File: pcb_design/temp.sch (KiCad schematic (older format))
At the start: 3 parts

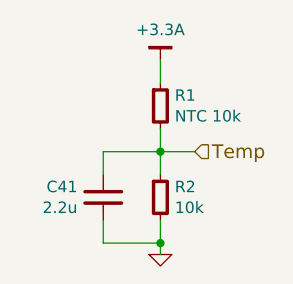
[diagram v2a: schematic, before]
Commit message: Completed some part numbers
Signed-off-by: Marcos Chaparro <mchaparro@paltatech.com>
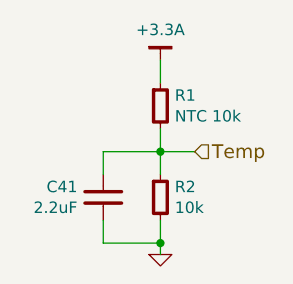
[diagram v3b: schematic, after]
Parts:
- C41: value 2.2u -> 2.2uF; MFR (none) -> Murata Electronics North America; MPN (none) -> GRM188R71A225KE15D; SPN (none) -> 490-4520-1-ND; SPR (none) -> Digikey
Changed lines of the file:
@@
 U 1 1 5426DB25
 P 4400 4200
-F 0 "#PWR38" H 4400 4200 30  0001 C CNN
-F 1 "GND" H 4400 4130 30  0001 C CNN
-F 2 "" H 4400 4200 60  0000 C CNN
-F 3 "" H 4400 4200 60  0000 C CNN
+F 0 "#PWR38" H 4400 4200 30 0001 C CNN
+F 1 "GND" H 4400 4130 30 0001 C CNN
+F 2 "" H 4400 4200 60 0000 C CNN
+F 3 "" H 4400 4200 60 0000 C CNN
 	1    4400 4200
 	1    0    0    -1
 $EndComp
-Wire Wire Line
-	4400 4050 4400 4200
-Wire Wire Line
-	4150 4150 4400 4150
-Connection ~ 4400 4150
-Wire Wire Line
-	4400 3650 4400 3850
-Wire Wire Line
-	4150 3750 4550 3750
-Connection ~ 4400 3750
-Wire Wire Line
-	4400 3350 4400 3450
-Text HLabel 4550 3750 2    60   Input ~ 0
-Temp
 $Comp
 L R-0603 R2
 U 1 1 588BA5AA
 P 4400 3950
-F 0 "R2" H 4463 3996 50  0000 L CNN
-F 1 "10k" H 4463 3905 50  0000 L CNN
-F 2 "IPC7351-Nominal:RESC1608X50" H 4400 3950 50  0001 C CNN
-F 3 "" H 4400 4000 60  0000 C CNN
-F 4 "RES SMD 1k 5% [0603]" H 5150 4500 60  0001 C CNN "BOM"
+F 0 "R2" H 4463 3996 50 0000 L CNN
+F 1 "10k" H 4463 3905 50 0000 L CNN
+F 2 "IPC7351-Nominal:RESC1608X50" H 4400 3950 50 0001 C CNN
+F 3 "" H 4400 4000 60 0000 C CNN
+F 4 "RES SMD 1k 5% [0603]" H 5150 4500 60 0001 C CNN "BOM"
+F 5 "" H 0 0 50 0001 C CNN "MFR"
+F 6 "" H 0 0 50 0001 C CNN "MPN"
+F 7 "" H 0 0 50 0001 C CNN "SPR"
+F 8 "" H 0 0 50 0001 C CNN "SPN"
+F 9 "" H 0 0 50 0001 C CNN "SPURL"
 	1    4400 3950
 	1    0    0    -1
@@
 U 1 1 588BA6A5
 P 4400 3550
-F 0 "R1" H 4463 3596 50  0000 L CNN
-F 1 "NTC 10k" H 4463 3505 50  0000 L CNN
-F 2 "IPC7351-Nominal:RESC1608X50" H 4400 3550 50  0001 C CNN
-F 3 "" H 4400 3600 60  0000 C CNN
-F 4 "RES SMD 1k 5% [0603]" H 5150 4100 60  0001 C CNN "BOM"
+F 0 "R1" H 4463 3596 50 0000 L CNN
+F 1 "NTC 10k" H 4463 3505 50 0000 L CNN
+F 2 "IPC7351-Nominal:RESC1608X50" H 4400 3550 50 0001 C CNN
+F 3 "" H 4400 3600 60 0000 C CNN
+F 4 "RES SMD 1k 5% [0603]" H 5150 4100 60 0001 C CNN "BOM"
+F 5 "" H 0 0 50 0001 C CNN "MFR"
+F 6 "" H 0 0 50 0001 C CNN "MPN"
+F 7 "" H 0 0 50 0001 C CNN "SPR"
+F 8 "" H 0 0 50 0001 C CNN "SPN"
+F 9 "" H 0 0 50 0001 C CNN "SPURL"
 	1    4400 3550
 	1    0    0    -1
@@
 U 1 1 588BA7A2
 P 4150 3950
-F 0 "C41" H 4263 3996 50  0000 L CNN
-F 1 "2.2u" H 4263 3905 50  0000 L CNN
-F 2 "IPC7351-Nominal:CAPC1608X55" H 4150 3950 50  0001 C CNN
-F 3 "" H 4140 3925 60  0000 C CNN
-F 4 "CAP MLCC 100pF C0G 50V 5% [0603]" H 4950 4500 60  0001 C CNN "BOM"
+F 0 "C41" H 4263 3996 50 0000 L CNN
+F 1 "2.2uF" H 4263 3905 50 0000 L CNN
+F 2 "IPC7351-Nominal:CAPC1608X55" H 4150 3950 50 0001 C CNN
+F 3 "http://www.murata.com/~/media/webrenewal/support/library/catalog/products/capacitor/mlcc/c02e.ashx" H 4140 3925 60 0001 C CNN
+F 4 "CAP MLCC 100pF C0G 50V 5% [0603]" H 4950 4500 60 0001 C CNN "BOM"
+F 5 "Murata Electronics North America" H 0 0 50 0001 C CNN "MFR"
+F 6 "GRM188R71A225KE15D" H 0 0 50 0001 C CNN "MPN"
+F 7 "Digikey" H 0 0 50 0001 C CNN "SPR"
+F 8 "490-4520-1-ND" H 0 0 50 0001 C CNN "SPN"
+F 9 "" H 0 0 50 0001 C CNN "SPURL"
 	1    4150 3950
 	-1   0    0    -1
 $EndComp
+$Comp
+L +3.3A #PWR37
+U 1 1 588BA405
+P 4400 3350
+F 0 "#PWR37" H 0 100 30 0001 C CNN
+F 1 "+3.3A" H 4400 3483 50 0000 C CNN
+F 2 "" H 0 50 60 0000 C CNN
+F 3 "" H 0 50 60 0000 C CNN
+	1    4400 3350
+	1    0    0    -1
+$EndComp
+Text HLabel 4550 3750 2    60   Input ~ 0
+Temp
+Wire Wire Line
+	4400 4050 4400 4200
+Wire Wire Line
+	4150 4150 4400 4150
+Wire Wire Line
+	4400 3650 4400 3850
+Wire Wire Line
+	4150 3750 4550 3750
+Wire Wire Line
+	4400 3350 4400 3450
 Wire Wire Line
 	4150 3850 4150 3750
 Wire Wire Line
 	4150 4050 4150 4150
-$Comp
-L +3.3A #PWR37
-U 1 1 588BA405
-P 4400 3350
-F 0 "#PWR37" H 0   100 30  0001 C CNN
-F 1 "+3.3A" H 4400 3483 50  0000 C CNN
-F 2 "" H 0   50  60  0000 C CNN
-F 3 "" H 0   50  60  0000 C CNN
-	1    4400 3350
-	1    0    0    -1
-$EndComp
+Connection ~ 4400 4150
+Connection ~ 4400 3750
 $EndSCHEMATC

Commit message: Completed part number, manufacturer, etc fields. Simulated analog conditioning
Signed-off-by: Marcos Chaparro <mchaparro@paltatech.com>
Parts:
- R1: MFR (none) -> Murata Electronics North America; MPN (none) -> NCP18XH103F03RB; SPN (none) -> 490-4800-1-ND; SPR (none) -> Digikey
- R2: MFR (none) -> Yageo; MPN (none) -> RC0603FR-0710KL; SPN (none) -> 311-10.0KHRCT-ND; SPR (none) -> Digikey
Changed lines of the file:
@@
 F 1 "10k" H 4463 3905 50 0000 L CNN
 F 2 "IPC7351-Nominal:RESC1608X50" H 4400 3950 50 0001 C CNN
-F 3 "" H 4400 4000 60 0000 C CNN
+F 3 "" H 4400 4000 60 0001 C CNN
 F 4 "RES SMD 1k 5% [0603]" H 5150 4500 60 0001 C CNN "BOM"
-F 5 "" H 0 0 50 0001 C CNN "MFR"
-F 6 "" H 0 0 50 0001 C CNN "MPN"
-F 7 "" H 0 0 50 0001 C CNN "SPR"
-F 8 "" H 0 0 50 0001 C CNN "SPN"
+F 5 "Yageo" H 0 0 50 0001 C CNN "MFR"
+F 6 "RC0603FR-0710KL" H 0 0 50 0001 C CNN "MPN"
+F 7 "Digikey" H 0 0 50 0001 C CNN "SPR"
+F 8 "311-10.0KHRCT-ND" H 0 0 50 0001 C CNN "SPN"
 F 9 "" H 0 0 50 0001 C CNN "SPURL"
 	1    4400 3950
@@
 F 1 "NTC 10k" H 4463 3505 50 0000 L CNN
 F 2 "IPC7351-Nominal:RESC1608X50" H 4400 3550 50 0001 C CNN
-F 3 "" H 4400 3600 60 0000 C CNN
+F 3 "" H 4400 3600 60 0001 C CNN
 F 4 "RES SMD 1k 5% [0603]" H 5150 4100 60 0001 C CNN "BOM"
-F 5 "" H 0 0 50 0001 C CNN "MFR"
-F 6 "" H 0 0 50 0001 C CNN "MPN"
-F 7 "" H 0 0 50 0001 C CNN "SPR"
-F 8 "" H 0 0 50 0001 C CNN "SPN"
+F 5 "Murata Electronics North America" H 0 0 50 0001 C CNN "MFR"
+F 6 "NCP18XH103F03RB" H 0 0 50 0001 C CNN "MPN"
+F 7 "Digikey" H 0 0 50 0001 C CNN "SPR"
+F 8 "490-4800-1-ND" H 0 0 50 0001 C CNN "SPN"
 F 9 "" H 0 0 50 0001 C CNN "SPURL"
 	1    4400 3550

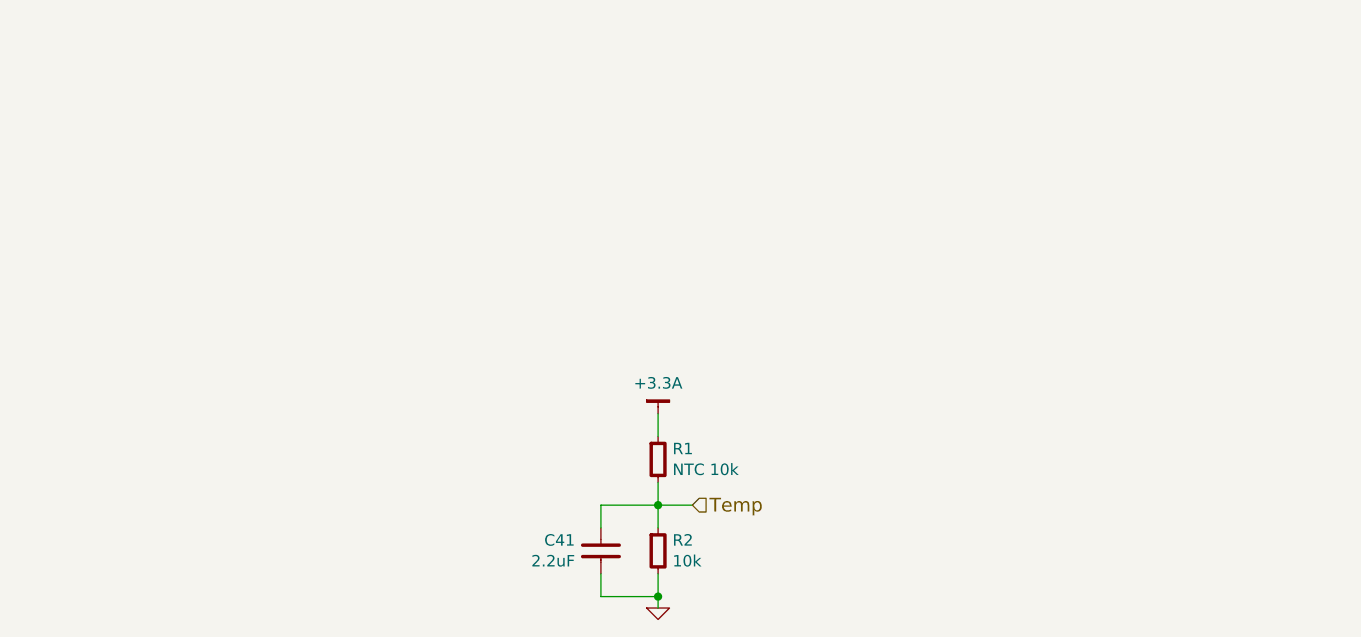
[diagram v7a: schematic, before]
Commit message: Added RC filter to FAULT line to prevent noise triggering it
Signed-off-by: Marcos Chaparro <mchaparro@paltatech.com>
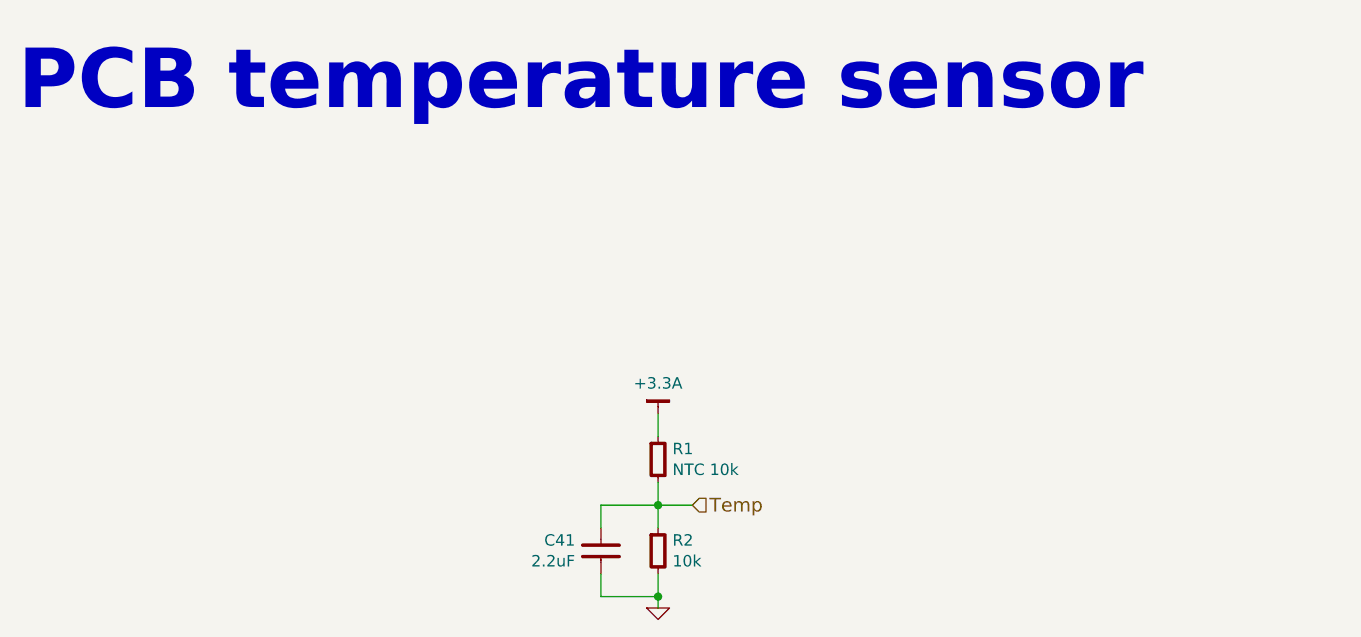
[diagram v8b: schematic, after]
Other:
- note added: "PCB temperature sensor"
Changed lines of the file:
@@
 Connection ~ 4400 4150
 Connection ~ 4400 3750
+Text Notes 1600 2050 0    260  ~ 52
+PCB temperature sensor
 $EndSCHEMATC
